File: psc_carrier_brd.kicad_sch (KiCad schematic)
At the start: 6 parts

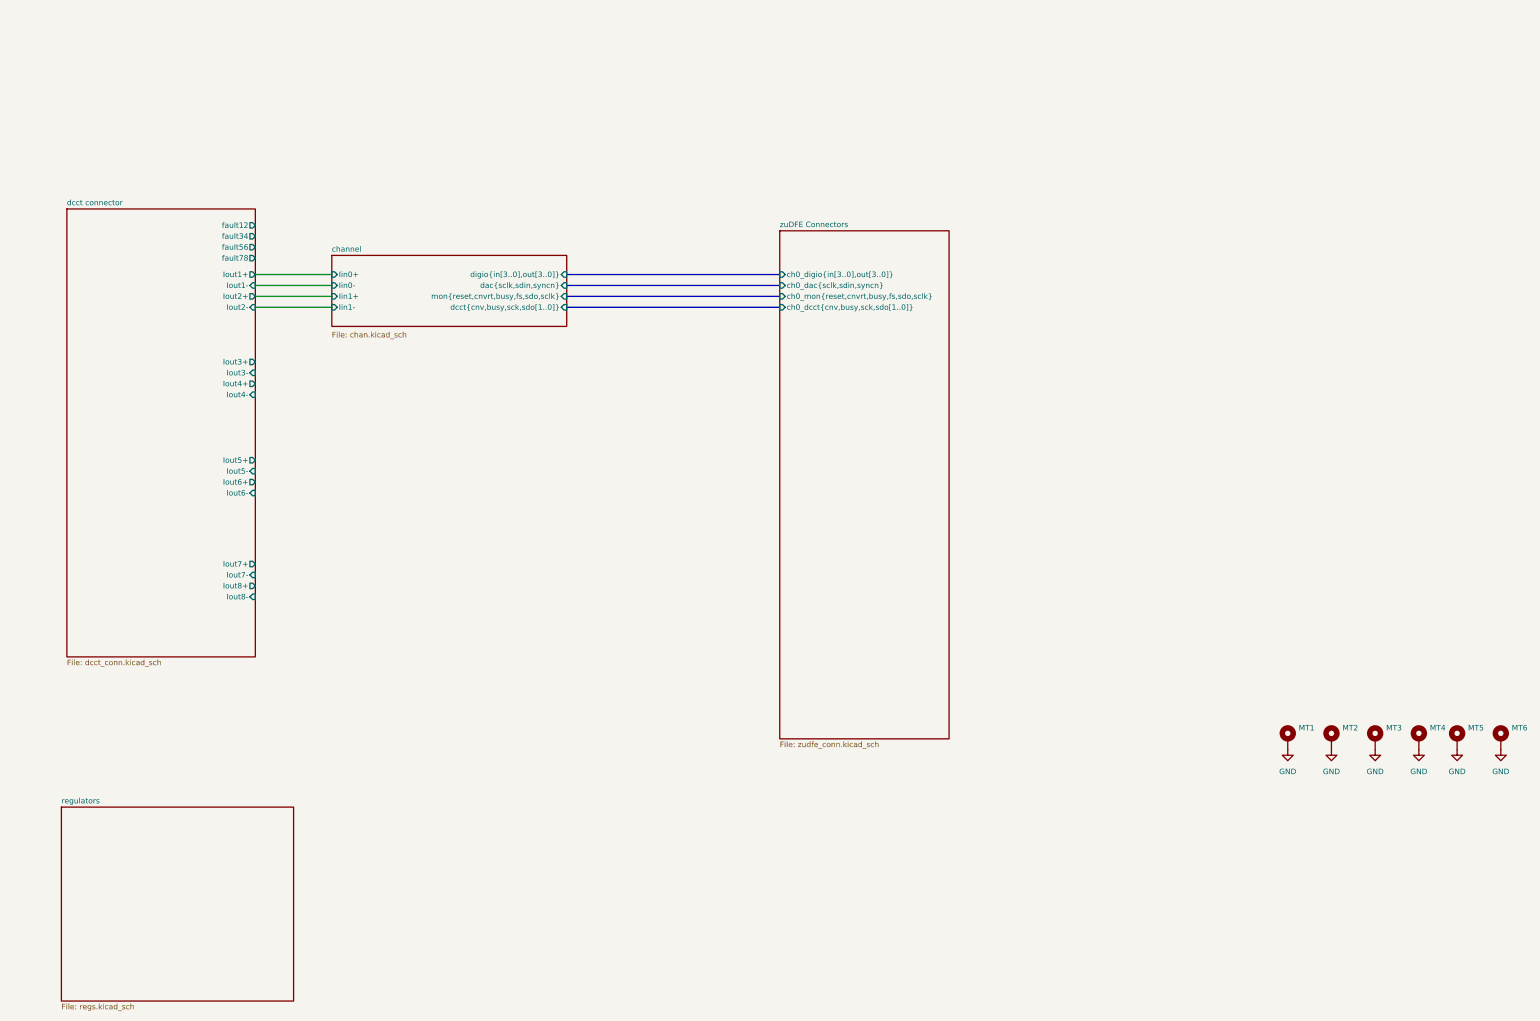
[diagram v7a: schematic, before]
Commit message: Add all 4 channels
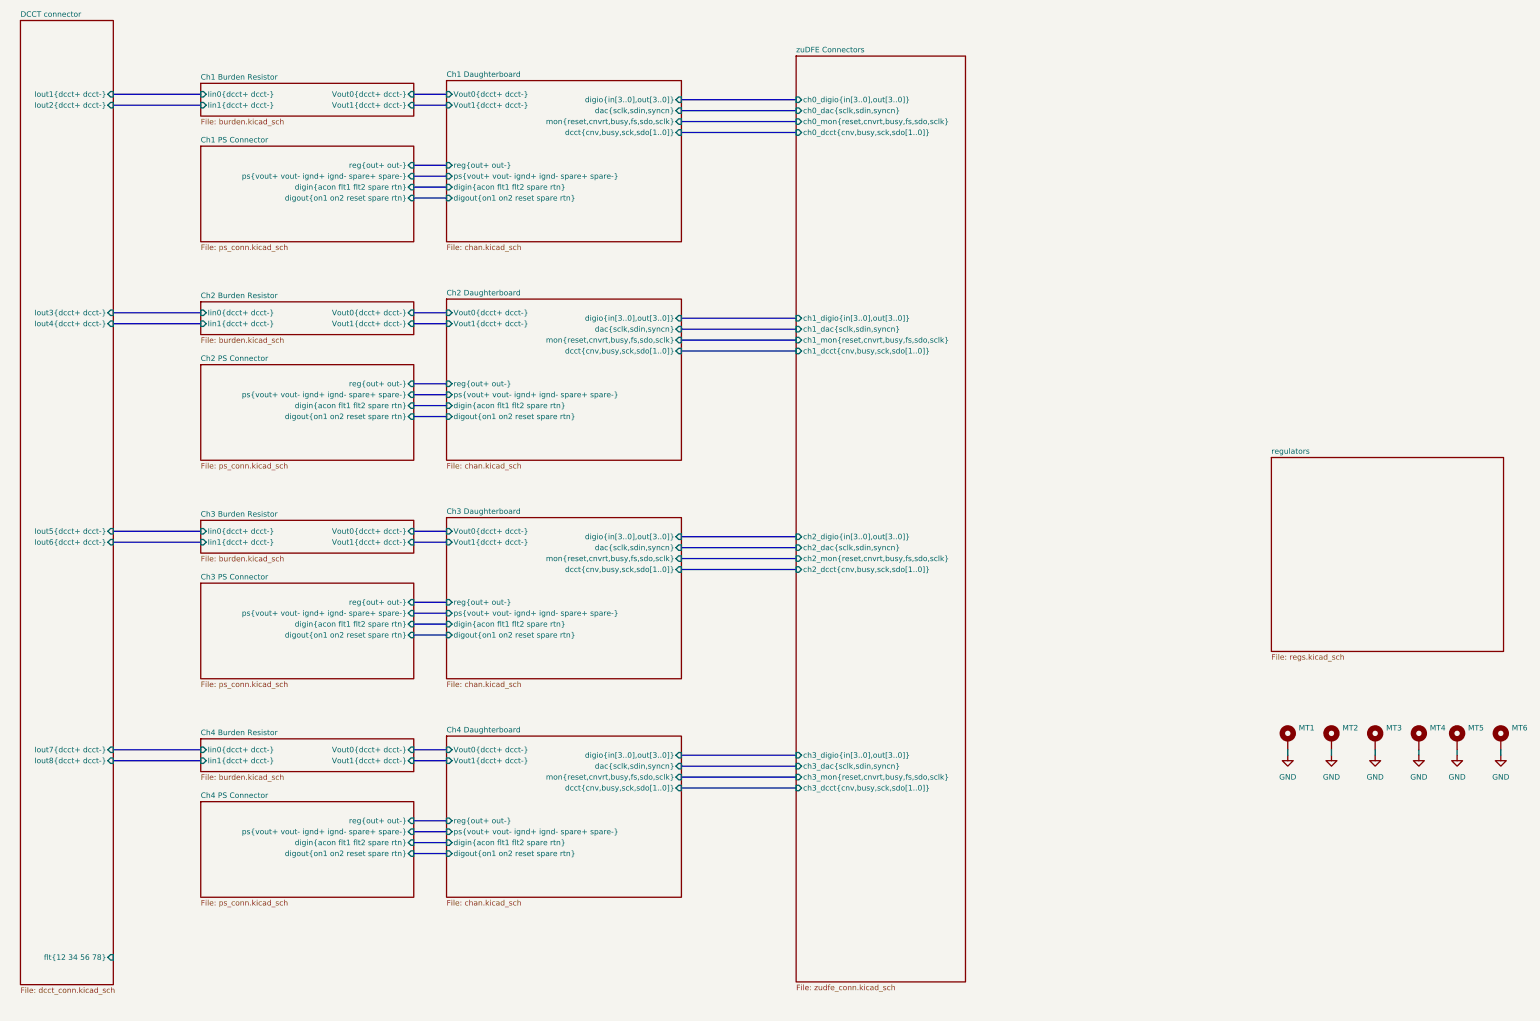
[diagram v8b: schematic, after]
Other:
- sheet channel renamed Ch1 Daughterboard
- sheet dcct connector renamed DCCT connector
- added sheet Ch1 Burden Resistor (burden.kicad_sch)
- added sheet Ch1 PS Connector (ps_conn.kicad_sch)
- added sheet Ch2 Burden Resistor (burden.kicad_sch)
- added sheet Ch2 Daughterboard (chan.kicad_sch)
- added sheet Ch2 PS Connector (ps_conn.kicad_sch)
- added sheet Ch3 Burden Resistor (burden.kicad_sch)
- added sheet Ch3 Daughterboard (chan.kicad_sch)
- added sheet Ch3 PS Connector (ps_conn.kicad_sch)
- added sheet Ch4 Burden Resistor (burden.kicad_sch)
- added sheet Ch4 Daughterboard (chan.kicad_sch)
- added sheet Ch4 PS Connector (ps_conn.kicad_sch)
- sheet Ch1 Daughterboard ports: added Vout0{dcct+ dcct-}, Vout1{dcct+ dcct-}, digin{acon flt1 flt2 spare rtn}, digout{on1 on2 reset spare rtn}, ps{vout+ vout- ignd+ ignd- spare+ spare-}, reg{out+ out-}; removed Iin0+, Iin0-, Iin1+, Iin1-
- sheet DCCT connector ports: added Iout1{dcct+ dcct-}, Iout2{dcct+ dcct-}, Iout3{dcct+ dcct-}, Iout4{dcct+ dcct-}, Iout5{dcct+ dcct-}, Iout6{dcct+ dcct-}, Iout7{dcct+ dcct-}, Iout8{dcct+ dcct-}, flt{12 34 56 78}; removed Iout1+, Iout1-, Iout2+, Iout2-, Iout3+, Iout3-, Iout4+, Iout4-, Iout5+, Iout5-, Iout6+, Iout6-, Iout7+, Iout7-, Iout8+, Iout8-, fault12, fault34, fault56, fault78
- sheet zuDFE Connectors ports: added ch1_dac{sclk,sdin,syncn}, ch1_dcct{cnv,busy,sck,sdo[1..0]}, ch1_digio{in[3..0],out[3..0]}, ch1_mon{reset,cnvrt,busy,fs,sdo,sclk}, ch2_dac{sclk,sdin,syncn}, ch2_dcct{cnv,busy,sck,sdo[1..0]}, ch2_digio{in[3..0],out[3..0]}, ch2_mon{reset,cnvrt,busy,fs,sdo,sclk}, ch3_dac{sclk,sdin,syncn}, ch3_dcct{cnv,busy,sck,sdo[1..0]}, ch3_digio{in[3..0],out[3..0]}, ch3_mon{reset,cnvrt,busy,fs,sdo,sclk}; removed none
